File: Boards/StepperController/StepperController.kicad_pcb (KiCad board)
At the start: 2 copper layers, 160 x 100 mm, 189 parts, among them IC1 ATMEGA645A-A, J1 I2C, J2 SPI_Extern, J3 ISP, J4 Reference, J5 Display, J6 Ext, J7 Spindle, P1 Power, P10 CONN_Z, P2 Cover, P3 USB_B, P4 Relay2, P5 Relay1, P6 Emer_Off, P8 CONN_X, P9 CONN_Y, Q1 BC817-40, Q2 BC817-40, Q3 BC817-40, Q4 BC817-40, Q5 BC817-40, Q6 BC807-40, Q7 BC807-40, Q8 BC817-40, SW2 SW_1, SW3 SW_2, U1 LM2576S-5, U2 74HC11, U3 FT232RL, U4 74HC08, U5 TMC2660, U6 TMC2660, U7 TMC2660, X1 16MHz, Y1 20MHz

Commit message: Minor Layout changes
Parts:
- removed the REF** at (84.8, 79.2)
- added REF***: OSHW-Logo_7.5x8mm_SilkScreen, Symbols:OSHW-Logo_7.5x8mm_SilkScreen, F.Cu at (219.1, 141.0)
- R52, R53, R54, R55, R58, R60: value 10R -> 100R
- R61, R62, R63, R64, R66: value 270R -> 160R
- moved G*** 5.79 mm to (148.0, 119.4)
- moved C4 1.14 mm to (127.6, 126.7)
- moved C6 0.76 mm to (120.7, 121.4)
- moved C7 0.76 mm to (113.3, 130.8)
- moved C5 0.64 mm to (120.0, 129.3)
- turned Q6 to 270 degrees
- turned Q7 to 270 degrees
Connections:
- J5 pad 7: (no net) -> GND
- Q6 pad 2: Net-(Q6-Pad2) -> +5V
- Q6 pad 3: +5V -> Net-(Q6-Pad3)
- Q7 pad 2: Net-(Q7-Pad2) -> +5V
- Q7 pad 3: +5V -> Net-(Q7-Pad3)
- R61 pad 2: Net-(Q6-Pad2) -> Net-(Q6-Pad3)
- R63 pad 1: Net-(Q7-Pad2) -> Net-(Q7-Pad3)
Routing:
- net Net-(Q7-Pad2): track 4.13 -> 0.00 mm
- net /Controller/Cover: track 63.8 -> 67.6 mm
- net Net-(Q6-Pad2): track 3.23 -> 0.00 mm
- net Net-(Q7-Pad3): track 0.00 -> 3.15 mm
- net Net-(Q6-Pad3): track 0.00 -> 2.84 mm
- net +5V: track 743.3 -> 745.5 mm
- net /Controller/Emergency_Off: track 59.9 -> 61.8 mm
- net GND: track 238.8 -> 240.0 mm

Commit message: Version 0.0.1
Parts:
- RL1, RL2: value FINDER-36.11.4001 -> FINDER-36.11-4301; footprint Relays_ThroughHole:Relay_SPDT_SingleRow_Standing_FinderType34Point51 -> w_relay:relay_SJ-1M
- moved D5 7.15 mm to (78.1, 85.7), turned to 0 degrees
- moved RL1 6.61 mm to (78.1, 73.7), turned to 180 degrees
- moved RL2 6.60 mm to (91.9, 73.7), turned to 180 degrees
- moved C41 1.27 mm to (125.2, 86.9)
- moved C24 0.63 mm to (191.1, 95.5)
- moved SW2 0.63 mm to (161.5, 149.4)
- moved SW3 0.63 mm to (174.8, 149.4)
- moved C21 0.53 mm to (191.5, 86.9)
- moved C31 0.51 mm to (158.0, 86.9)
- moved C44 0.51 mm to (124.5, 95.5)
- moved D20 0.51 mm to (190.2, 144.0)
- moved C34 0.13 mm to (157.1, 95.5)
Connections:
- P4 pad 1: Net-(P4-Pad1) -> (no net)
- P4 pad 2: Net-(P4-Pad2) -> (no net)
- RL1 pad 11: Net-(P5-Pad1) -> Net-(P5-Pad2)
- RL1 pad 14: Net-(P5-Pad2) -> Net-(P5-Pad1)
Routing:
- net Net-(P4-Pad1): track 19.5 -> 0.00 mm
- net Net-(P4-Pad2): track 11.6 -> 0.00 mm
- net Net-(P5-Pad1): track 19.1 -> 8.71 mm
- net Net-(D30-Pad1): track 10.8 -> 19.3 mm
- net Net-(P3-Pad2): track 18.2 -> 21.1 mm
- net Net-(P3-Pad3): track 22.5 -> 24.9 mm
- net +5V: track 745.5 -> 747.5 mm
- net VSA: track 222.4 -> 223.5 mm
- net Net-(C15-Pad1): track 51.2 -> 50.2 mm
- net /Controller/SDO: track 233.8 -> 234.4 mm
- net Net-(P5-Pad2): track 11.8 -> 11.1 mm
- net Net-(P6-Pad2): track 5.81 -> 5.23 mm

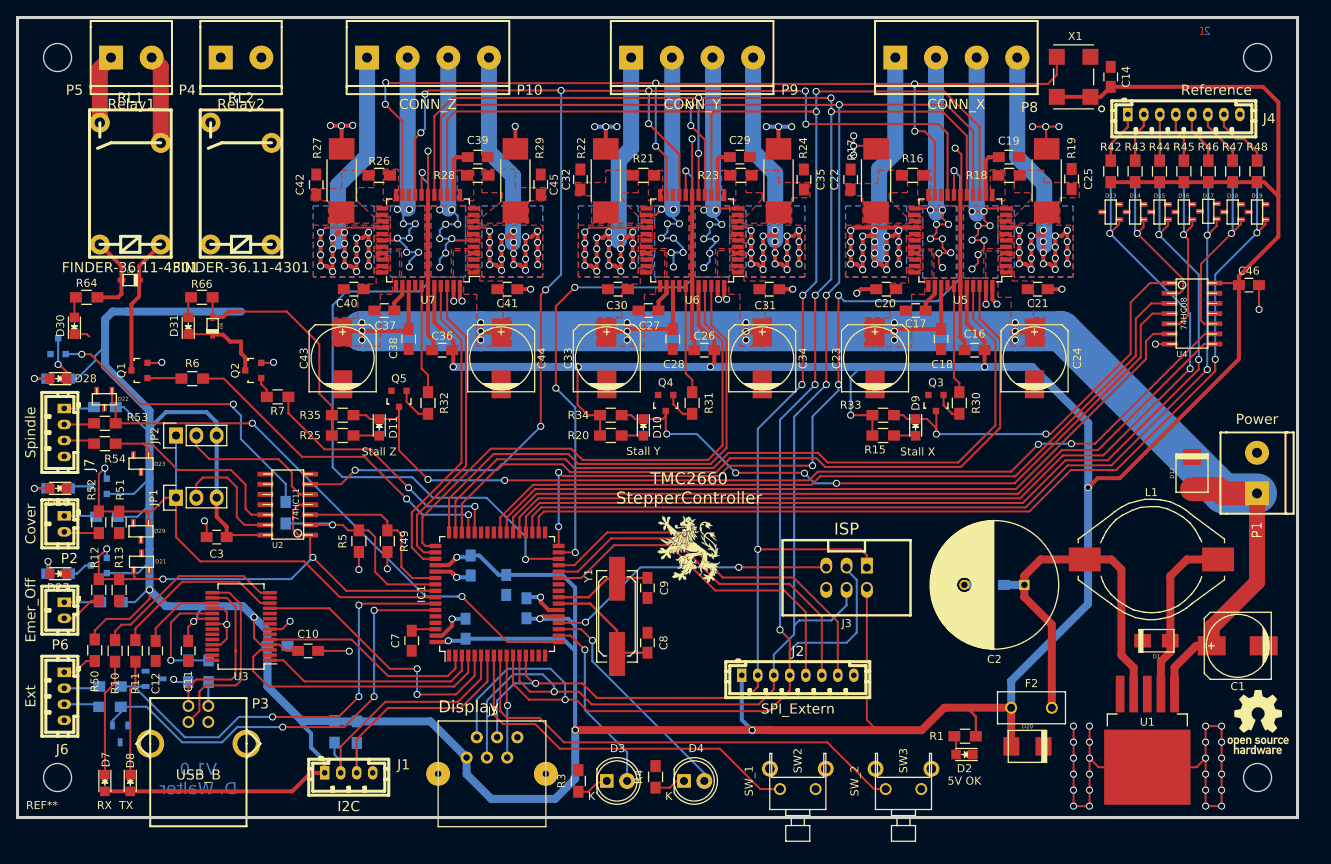
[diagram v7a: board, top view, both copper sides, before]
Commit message: Layout optimizations
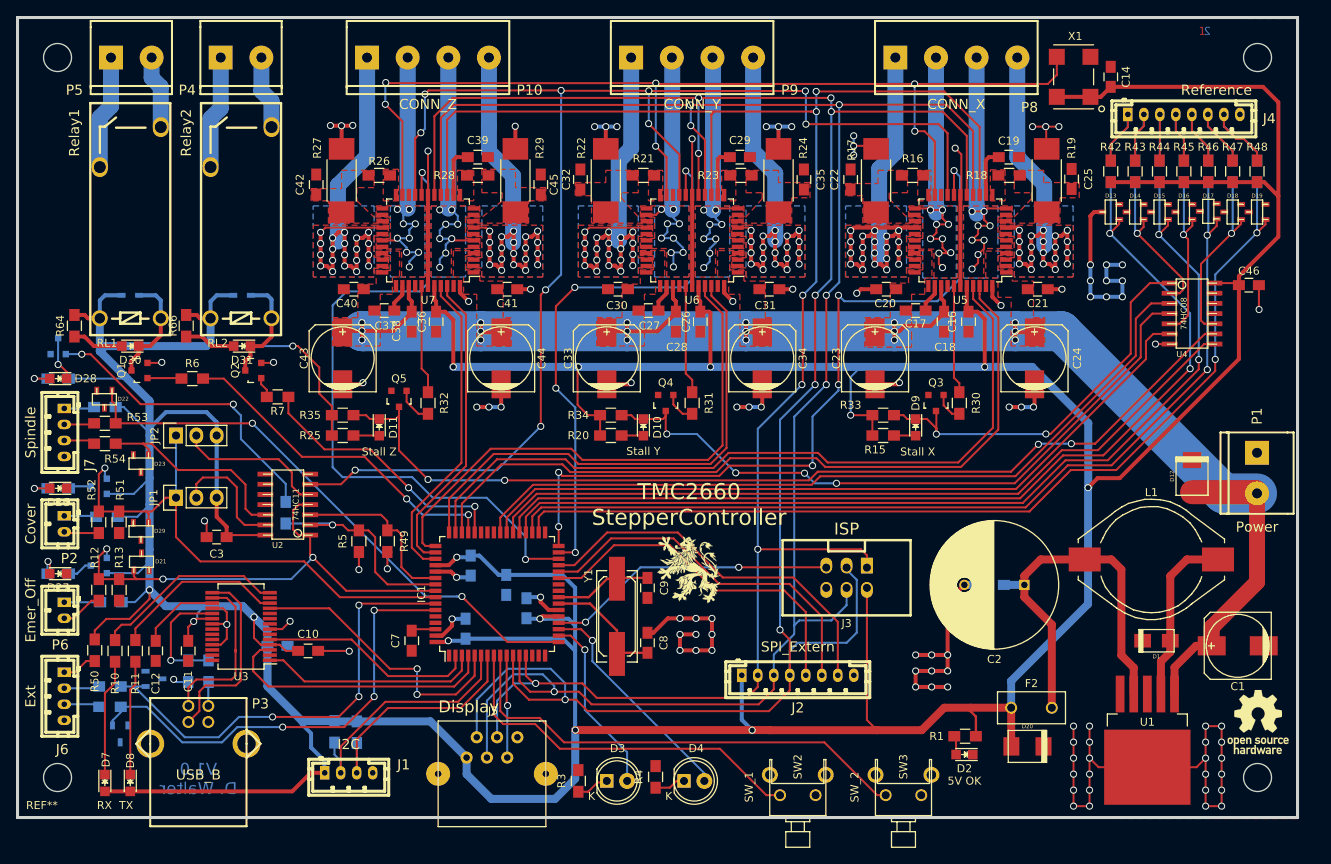
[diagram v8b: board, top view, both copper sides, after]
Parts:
- D5, D6: moved to B.Cu
- RL1, RL2: footprint w_relay:relay_SJ-1M -> Relais:Fujiutsu_JS-MT
- moved D30 7.43 mm to (78.1, 94.0), turned to 180 degrees
- moved D31 7.19 mm to (92.1, 94.0), turned to 180 degrees
- moved D6 5.30 mm to (92.1, 87.6), turned to 0 degrees
- moved RL1 4.45 mm to (78.1, 78.1), turned to 0 degrees
- moved RL2 4.45 mm to (91.9, 78.1), turned to 0 degrees
- moved R66 4.06 mm to (85.1, 91.4), turned to 270 degrees
- moved R64 3.87 mm to (71.1, 91.4), turned to 270 degrees
- moved C16 3.64 mm to (182.9, 90.9), turned to 270 degrees
- moved C36 3.64 mm to (116.3, 90.9), turned to 270 degrees
- moved C26 3.59 mm to (149.4, 90.9), turned to 270 degrees
- moved G*** 2.54 mm to (148.0, 121.9)
- moved C18 2.19 mm to (179.8, 90.9)
- moved C28 2.19 mm to (146.3, 90.9)
- moved C38 2.19 mm to (113.3, 90.9)
- moved D5 1.91 mm to (78.1, 87.6)
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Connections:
- P1 pad 1: VSA -> GND
- P1 pad 2: GND -> VSA
- P4 pad 1: (no net) -> Net-(P4-Pad1)
- P4 pad 2: (no net) -> Net-(P4-Pad2)
- RL1 pad 11: Net-(P5-Pad2) -> Net-(P5-Pad1)
- RL1 pad 14: Net-(P5-Pad1) -> Net-(P5-Pad2)
- SW2 pad 3: (no net) -> GND
- SW3 pad 3: (no net) -> GND
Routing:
- net GND: track 239.8 -> 307.5 mm, vias 67 -> 103
- net Net-(P4-Pad1): track 0.00 -> 14.2 mm
- net Net-(P4-Pad2): track 0.00 -> 9.22 mm
- net Net-(P5-Pad1): track 8.71 -> 14.3 mm
- net Net-(D30-Pad1): track 19.3 -> 14.1 mm
- net Net-(D30-Pad2): track 2.58 -> 6.43 mm
- net +5V: track 747.5 -> 751.0 mm, vias 14 -> 15
- net Net-(D31-Pad2): track 3.14 -> 6.43 mm
- net Net-(D31-Pad1): track 10.8 -> 13.9 mm
- net VSA: track 223.5 -> 221.4 mm
- net Net-(P5-Pad2): track 11.1 -> 9.17 mm
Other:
- board text added: "High Voltage!"
